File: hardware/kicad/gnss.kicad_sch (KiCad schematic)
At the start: 11 parts, among them U11 TXB0106PWR, U7 L76L-M33

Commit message: update bill of materials
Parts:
- C13, C14: Distributor Link https://www.lcsc.com/product-detail/Multilayer-Ceramic-Capacitors-MLCC-SMD-SMT_Samsung-Electro-Mechanics-CL10A106KP8NNNC_C19702.html -> https://www.lcsc.com/product-detail/Multilayer-Ceramic-Capacitors-MLCC-SMD-SMT_YAGEO-CC0603JRNPO9BN330_C107047.html; Distributor Part Number C19702 -> C107047; Id 1 -> (none); Manufacture Samsung Electro-Mechanics -> (none); Manufacture Part Number CL10A106KP8NNNC -> (none); Manufacturer (none) -> YAGEO; Manufacturer Part Number (none) -> CC0603JRNPO9BN330; Type SMD -> (none)
- C39, C40, C41: Distributor Link https://www.lcsc.com/product-detail/Multilayer-Ceramic-Capacitors-MLCC-SMD-SMT_Samsung-Electro-Mechanics-CL10A106KP8NNNC_C19702.html -> https://www.lcsc.com/product-detail/Multilayer-Ceramic-Capacitors-MLCC-SMD-SMT_Samsung-Electro-Mechanics-CL10B104KO8NNNC_C66501.html; Distributor Part Number C19702 -> C66501; Id 1 -> (none); Manufacture Samsung Electro-Mechanics -> (none); Manufacture Part Number CL10A106KP8NNNC -> (none); Manufacturer (none) -> Samsung Electro-Mechanics; Manufacturer Part Number (none) -> CL10B104KO8NNNC; Type SMD -> (none)
- C42: Id 1 -> (none); Manufacture Samsung Electro-Mechanics -> (none); Manufacture Part Number CL10A106KP8NNNC -> (none); Manufacturer (none) -> Samsung Electro-Mechanics; Manufacturer Part Number (none) -> CL10A106KP8NNNC; Type SMD -> (none)
- C43: Distributor Link https://www.lcsc.com/product-detail/Multilayer-Ceramic-Capacitors-MLCC-SMD-SMT_Samsung-Electro-Mechanics-CL10A106KP8NNNC_C19702.html -> https://www.lcsc.com/product-detail/Multilayer-Ceramic-Capacitors-MLCC-SMD-SMT_Samsung-Electro-Mechanics-CL10A475KP8NNNC_C1705.html; Distributor Part Number C19702 -> C1705; Id 1 -> (none); Manufacture Samsung Electro-Mechanics -> (none); Manufacture Part Number CL10A106KP8NNNC -> (none); Manufacturer (none) -> Samsung Electro-Mechanics; Manufacturer Part Number (none) -> CL10A475KP8NNNC; Type SMD -> (none)
- D8: footprint Capacitor_SMD:C_0402_1005Metric -> Diode_SMD:D_SOD-882; Distributor (none) -> LCSC; Distributor Part Number (none) -> C5173251; Manufacturer (none) -> Leiditech; Manufacturer Part Number (none) -> ESD5651N
- U11: Distributor (none) -> LCSC; Distributor Link (none) -> https://www.lcsc.com/product-detail/Translators-Level-Shift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; Distributor Part Number (none) -> C38253; Manufacturer (none) -> Texas Instruments; Manufacturer Part Number (none) -> TXB0106PWR
- U7: Distributor (none) -> DigiKey; Distributor Link (none) -> https://www.digikey.com/en/products/detail/quectel/L76L-M33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; Distributor Part Number (none) -> 2958-L76L-M33CT-ND; Manufacturer (none) -> Quectel; Manufacturer Part Number (none) -> L76L-M33
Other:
- note added: "- Acquisition : 30mA @VCC=V_BCKP=3.3V (GPS+GLONASS) - Tracking : 26mA @VCC=V_BCKP=3.3V (GPS+GLONASS) - Standby : 1mA @VCC=V_BCKP=3.3V - Backup : 7uA @V_BCKP=3.3V"
- note added: "GNSS System Band Frequency ---------------------------------------- GPS L1 C/A 1574.397-1576.443 MHz BeiDou B1I 1559.052-1563.144 MHz GLONASS L1 1597.781-1605.656 MHz Galileo E1 1573.374-1577.466 MHz QZSS L1 C/A 1574.397-1576.443 MHz"
- note added: "L76L-M33 Frequency"
- note added: "Power Profile"
- note added: "not used for passive antenna"
- note added: "note: the lowest value capacitor should be the closest to module pins."
- note removed: "- Acquisition: 30mA @VCC=V_BCKP=3.3V (GPS+GLONASS) - Tracking : 26mA @VCC=V_BCKP=3.3V (GPS+GLONASS) - Standby : 1mA @VCC=V_BCKP=3.3V - Backup : 7uA @V_BCKP=3.3V"
- note removed: "VCC_RF not used for passive antenna"

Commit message: add page info
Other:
- company: (none) -> Teapot Laboratories
- title: (none) -> GNSS
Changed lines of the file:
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@@
 	(generator_version "8.0")
 	(paper "A4")
+	(title_block
+		(title "GNSS")
+		(date "2024-05-17")
+		(rev "1")
+		(company "Teapot Laboratories")
+	)
 	(junction
 		(at 151.765 62.23)

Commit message: Start Rev 3
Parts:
- removed C13, C14: 33p, Capacitor_SMD:C_0603_1608Metric, symbol Device:C_Small
- removed C39, C40, C41: 100n, Capacitor_SMD:C_0603_1608Metric, symbol Device:C_Small
- removed C42: 10u, Capacitor_SMD:C_0603_1608Metric, symbol Device:C_Small
- removed C43: 4u7, Capacitor_SMD:C_0603_1608Metric, symbol Device:C_Small
- removed D8: ESD5651N, Diode_SMD:D_SOD-882, symbol Device:D_TVS
- removed JP1: SolderJumper_3_Bridged12, Jumper:SolderJumper-3_P1.3mm_Bridged2Bar12_RoundedPad1.0x1.5mm, symbol Jumper:SolderJumper_3_Bridged12
- removed U11: TXB0106PWR, bwlc1a:TSSOP-16_L5.0-W4.4-P0.65-LS6.4-BL, symbol bwlc1a:TXB0106PWR
- removed U7: L76L-M33, bwlc1a:L76L-M33, symbol bwlc1a:L76L-M33
- added U13: L96-M33, bwlc1a:L96-M33, symbol bwlc1a:L96-M33
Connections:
- new net: U13.10 (GND), U13.11 (GND), U13.12 (GND), U13.13 (GND), U13.14 (GND), U13.15 (GND), U13.18 (GND), U13.19 (GND), U13.21 (GND), U13.22 (GND), U13.27 (GND), U13.31 (GND), U13.4 (GND), U13.5 (GND)
- no-connect marks 7 -> 0
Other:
- note removed: "3V3-to-2V8 Level Shifter"
- note removed: "not used for passive antenna"

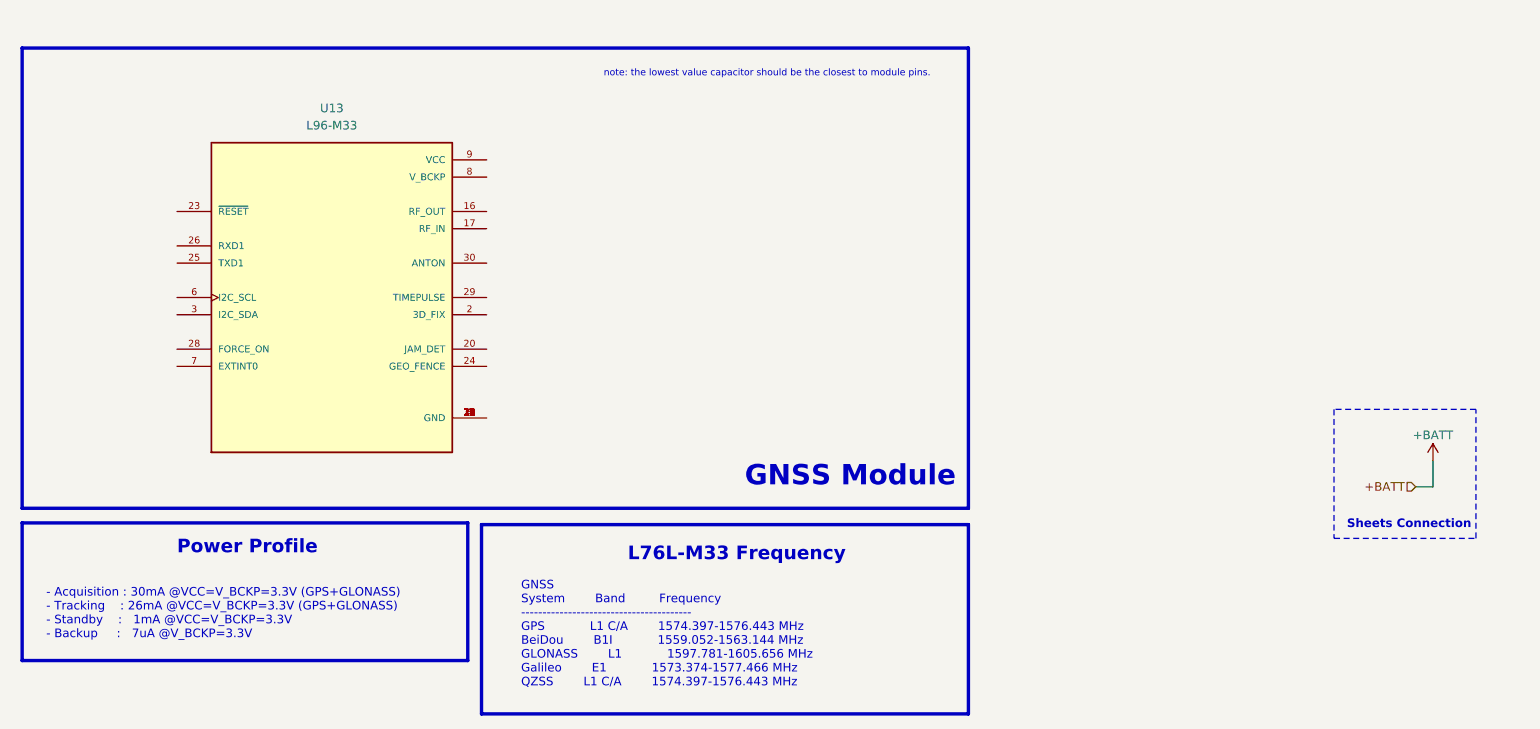
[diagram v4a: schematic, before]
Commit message: GNSS and Antenna Update
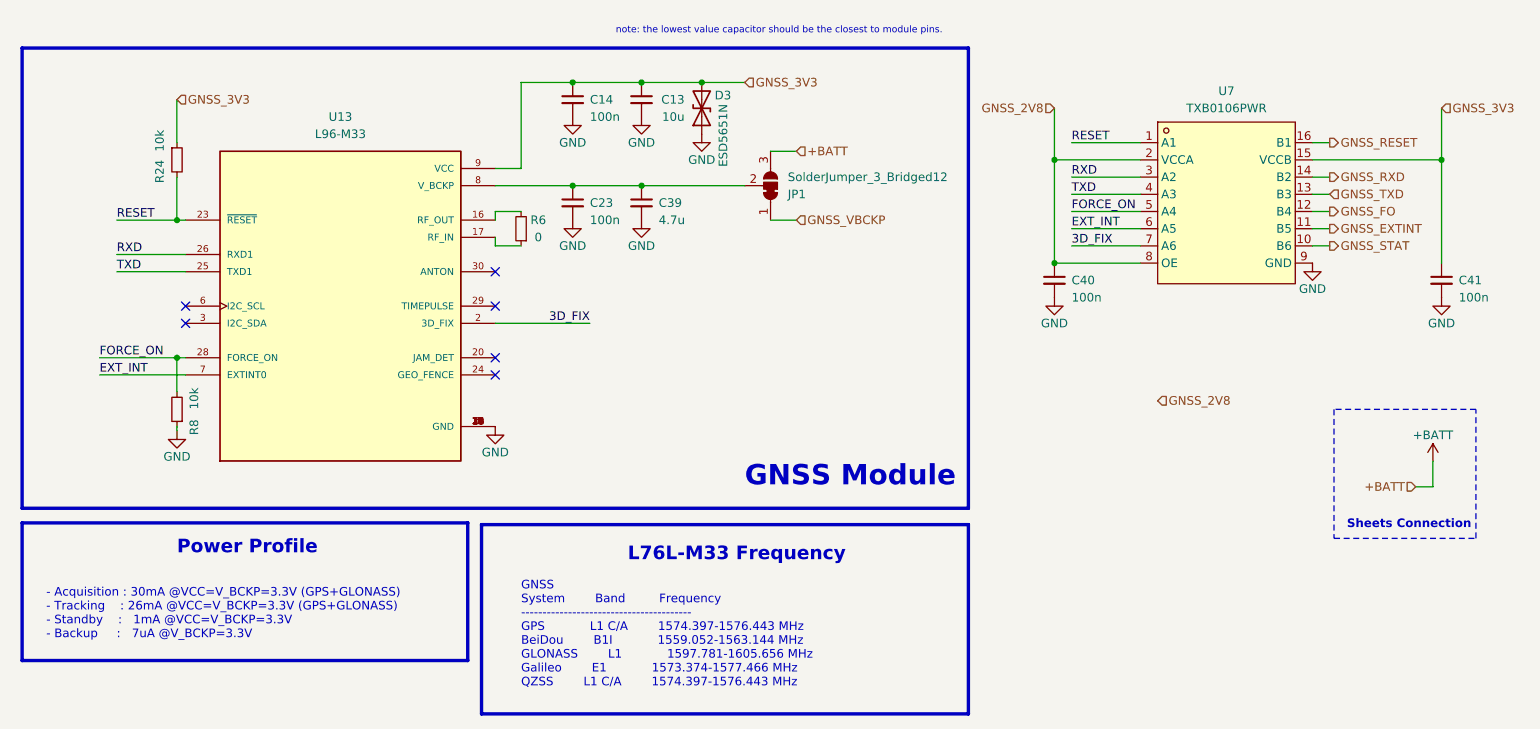
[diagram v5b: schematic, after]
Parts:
- added C13: 10u, Capacitor_SMD:C_0603_1608Metric, symbol Device:C_Small
- added C14, C23, C40, C41: 100n, Capacitor_SMD:C_0603_1608Metric, symbol Device:C_Small
- added C39: 4.7u, symbol Device:C_Small
- added D3: ESD5651N, Diode_SMD:D_SOD-882, symbol Device:D_TVS
- added JP1: SolderJumper_3_Bridged12, symbol Jumper:SolderJumper_3_Bridged12
- added R24, R8: 10k, Resistor_SMD:R_0402_1005Metric, symbol Device:R_Small
- added R6: 0, Resistor_SMD:R_0402_1005Metric, symbol Device:R_Small
- added U7: TXB0106PWR, bwlc1a:TSSOP-16_L5.0-W4.4-P0.65-LS6.4-BL, symbol bwlc1a:TXB0106PWR
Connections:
- net +BATT: now also JP1.3 (B)
- net GND: now reaches U13.10 (GND), U13.11 (GND), U13.12 (GND), U13.13 (GND), U13.14 (GND), U13.15 (GND), U13.18 (GND), U13.19 (GND), U13.21 (GND), U13.22 (GND), U13.27 (GND), U13.31 (GND), U13.4 (GND), U13.5 (GND)
- net GND: now also C13.2, C14.2, C23.2, C39.2, C40.2, C41.2, D3.1 (A1), R8.1, U7.9 (GND)
- net at U13.16 (RF_OUT): now also R6.2
- net at U13.17 (RF_IN): now also R6.1
- net 3D_FIX: now reaches U13.2 (3D_FIX)
- net 3D_FIX: now also U7.7 (A6)
- net RESET: now reaches U13.23 (~{RESET})
- net RESET: now also R24.2, U7.1 (A1)
- net TXD: now reaches U13.25 (TXD1)
- net TXD: now also U7.4 (A3)
- net RXD: now reaches U13.26 (RXD1)
- net RXD: now also U7.3 (A2)
- net FORCE_ON: now reaches U13.28 (FORCE_ON)
- net FORCE_ON: now also R8.2, U7.5 (A4)
- net EXT_INT: now reaches U13.7 (EXTINT0)
- net EXT_INT: now also U7.6 (A5)
- net at U13.8 (V_BCKP): now also C23.1, C39.1, JP1.2 (C)
- net GNSS_3V3: now reaches U13.9 (VCC)
- net GNSS_3V3: now also C13.1, C14.1, C41.1, D3.2 (A2), R24.1, U7.15 (VCCB)
- new net GNSS_2V8: C40.1, U7.2 (VCCA), U7.8 (OE)
- new net GNSS_EXTINT: U7.11 (B5)
- new net GNSS_FO: U7.12 (B4)
- new net GNSS_RESET: U7.16 (B1)
- new net GNSS_RXD: U7.14 (B2)
- new net GNSS_STAT: U7.10 (B6)
- new net GNSS_TXD: U7.13 (B3)
- new net GNSS_VBCKP: JP1.1 (A)
- no-connect marks 0 -> 6
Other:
- moved on the sheet: U13

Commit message: Update Sch for GNSS and main controller
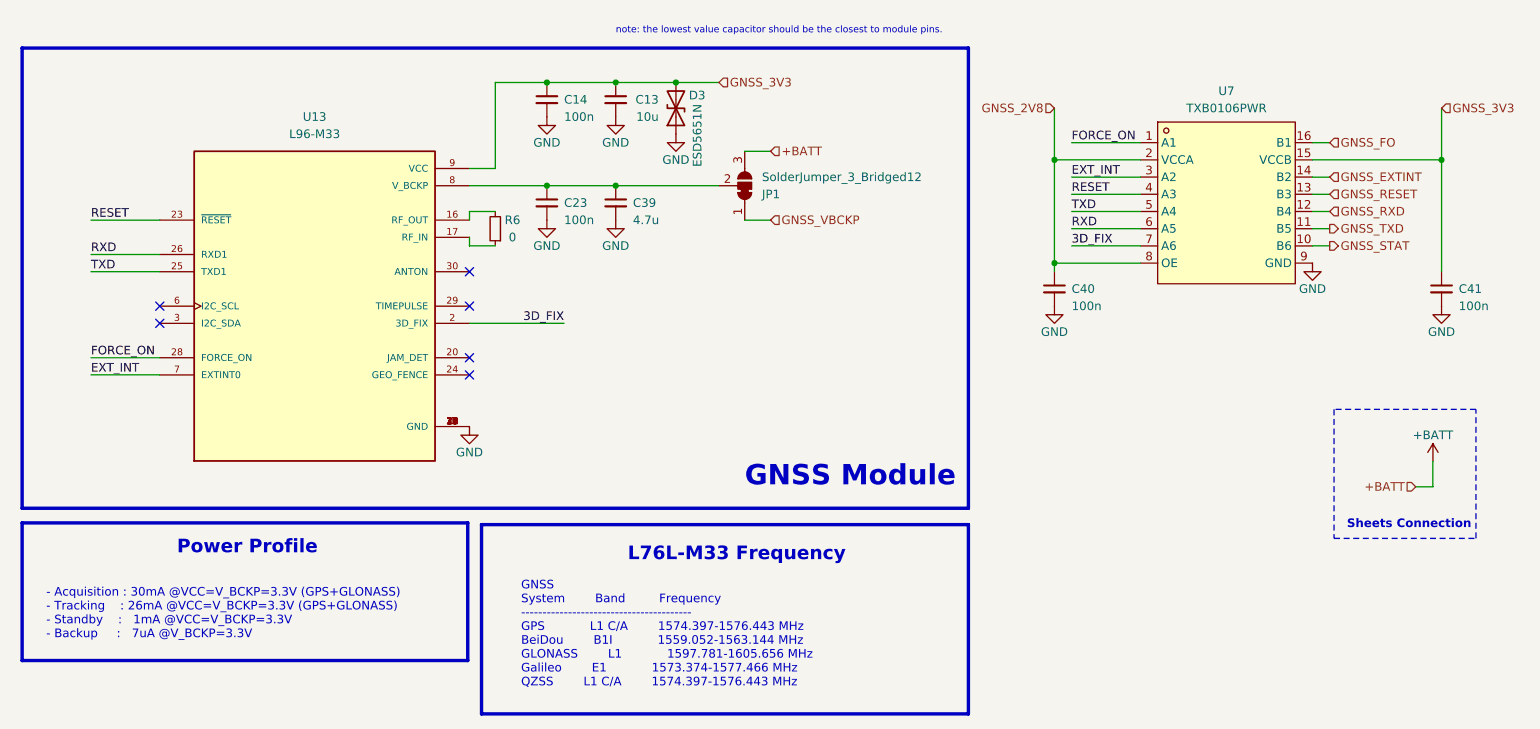
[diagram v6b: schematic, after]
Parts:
- removed R24, R8: 10k, Resistor_SMD:R_0402_1005Metric, symbol Device:R_Small
- C14, C23, C40, C41: footprint Capacitor_SMD:C_0603_1608Metric -> Capacitor_SMD:C_0402_1005Metric
- C39: footprint (none) -> Capacitor_SMD:C_0603_1608Metric
- JP1: footprint (none) -> Jumper:SolderJumper-3_P1.3mm_Bridged12_RoundedPad1.0x1.5mm
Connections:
- net EXT_INT: now also U7.3 (A2); no longer U7.6 (A5)
- net FORCE_ON: now also U7.1 (A1); no longer U7.5 (A4)
- net GNSS_EXTINT: now also U7.14 (B2); no longer U7.11 (B5)
- net GNSS_FO: now also U7.16 (B1); no longer U7.12 (B4)
- net GNSS_RESET: now also U7.13 (B3); no longer U7.16 (B1)
- net GNSS_RXD: now also U7.12 (B4); no longer U7.14 (B2)
- net GNSS_TXD: now also U7.11 (B5); no longer U7.13 (B3)
- net RESET: now also U7.4 (A3); no longer U7.1 (A1)
- net RXD: now also U7.6 (A5); no longer U7.3 (A2)
- net TXD: now also U7.5 (A4); no longer U7.4 (A3)
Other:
- moved on the sheet: C13, C14, C23, C39, C40, C41, D3, JP1, R6, U13

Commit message: Update for PCB Layout
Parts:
- removed C40, C41: 100n, Capacitor_SMD:C_0402_1005Metric, symbol Device:C_Small
- removed D3: ESD5651N, Diode_SMD:D_SOD-882, symbol Device:D_TVS
- removed U7: TXB0106PWR, bwlc1a:TSSOP-16_L5.0-W4.4-P0.65-LS6.4-BL, symbol bwlc1a:TXB0106PWR
- added D4: ESD5651N, Diode_SMD:D_SOD-882, symbol Device:D_TVS
- renumbered C14 to C12, C23 to C14, C39 to C15, R6 to R12, U13 to U2
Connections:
- net 3D_FIX is gone; now on net GNSS_STAT: U2.2 (3D_FIX)
- net EXT_INT is gone; now on net GNSS_EXTINT: U2.7 (EXTINT0)
- net FORCE_ON is gone; now on net GNSS_FO: U2.28 (FORCE_ON)
- net RESET is gone; now on net GNSS_RESET: U2.23 (~{RESET})
- net RXD is gone; now on net GNSS_RXD: U2.26 (RXD1)
- net TXD is gone; now on net GNSS_TXD: U2.25 (TXD1)
- net GND: now also D4.1 (A1)
- net GNSS_3V3: now also D4.2 (A2)
- net GNSS_JAMDET: now reaches U2.20 (JAM_DET)
- net GNSS_GEOFENCE: now reaches U2.24 (GEO_FENCE)
- no-connect marks 6 -> 4
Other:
- moved on the sheet: C12, C13, C14, C15, JP1, R12, U2

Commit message: Finish Manufacturing File
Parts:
- added TP21, TP22: GPIO46, TestPoint:TestPoint_Pad_D1.0mm, symbol Connector:TestPoint
- C12, C14: Distributor Link https://www.lcsc.com/product-detail/Multilayer-Ceramic-Capacitors-MLCC-SMD-SMT_Samsung-Electro-Mechanics-CL10B104KO8NNNC_C66501.html -> https://www.lcsc.com/product-detail/Multilayer-Ceramic-Capacitors-MLCC-SMD-SMT_Samsung-Electro-Mechanics-CL05B104KO5NNNC_C1525.html; Distributor Part Number C66501 -> C1525; Manufacturer Part Number CL10B104KO8NNNC -> CL05B104KO5NNNC
- C15: Distributor (none) -> LCSC; Distributor Link (none) -> https://www.lcsc.com/product-detail/Multilayer-Ceramic-Capa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; Distributor Part Number (none) -> C1705; Manufacturer (none) -> Samsung Electro-Mechanics; Manufacturer Part Number (none) -> CL10A475KP8NNNC
- U2: Distributor (none) -> Digikey; Distributor Link (none) -> https://www.digikey.com/en/products/detail/quectel/L96-M33/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; Distributor Part Number (none) -> 2958-L96-M33TR-ND; Manufacturer (none) -> Quectel; Manufacturer Part Number (none) -> L96-M33
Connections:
- net GNSS_GEOFENCE: now also TP22.1
- net GNSS_JAMDET: now also TP21.1
